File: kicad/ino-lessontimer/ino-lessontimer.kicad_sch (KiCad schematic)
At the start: 10 parts, among them SW1 BTNMinus, SW2 BTNPlus, SW3 BTNSet, SW4 BTNShow

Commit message: Updated schema to fixed TM1637
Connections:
- net +5V: now also U1.3 (VCC); no longer U1. (VCC)
- net GND: now also U1.4 (GND); no longer U1. (VCC)
- net at A1.5 (D2): now also U1.1 (CLK); no longer U1. (VCC)
- net at A1.6 (D3): now also U1.2 (DIO); no longer U1. (VCC)
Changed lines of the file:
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@@
     (stroke (width 0) (type default))
-  )
-  (symbol (lib_id "TM1637:TM1637") (at 107.95 73.66 0) (unit 1)
-    (in_bom yes) (on_board yes) (dnp no) (fields_autoplaced)
-    (property "Reference" "U1" (at 107.95 64.77 0)
-      (effects (font (size 1.27 1.27)))
-    )
-    (property "Value" "~" (at 107.95 73.66 0)
-      (effects (font (size 1.27 1.27)))
-    )
-    (property "Footprint" "" (at 107.95 73.66 0)
-      (effects (font (size 1.27 1.27)) hide)
-    )
-    (property "Datasheet" "" (at 107.95 73.66 0)
-      (effects (font (size 1.27 1.27)) hide)
-    )
-    (pin "")
-    (pin "")
-    (pin "")
-    (pin "")
-    (instances
-      (project "ino-lessontimer"
-        (path "/46ad6450-c889-484d-9737-a7f915eaad18"
-          (reference "U1") (unit 1)
-        )
-      )
-    )
   )
   (symbol (lib_id "Device:R") (at 107.95 101.6 90) (unit 1)
@@
         )
       )
+    )
+  )
+  (symbol (lib_id "TM1637:TM1637") (at 105.41 73.66 0) (unit 1)
+    (in_bom yes) (on_board yes) (dnp no) (fields_autoplaced)
+    (property "Reference" "U1" (at 105.41 64.77 0)
+      (effects (font (size 1.27 1.27)))
+    )
+    (property "Value" "~" (at 105.41 73.66 0)
+      (effects (font (size 1.27 1.27)))
+    )
+    (property "Footprint" "" (at 105.41 73.66 0)
+      (effects (font (size 1.27 1.27)) hide)
+    )
+    (property "Datasheet" "" (at 105.41 73.66 0)
+      (effects (font (size 1.27 1.27)) hide)
+    )
+    (pin "1")
+    (pin "2")
+    (pin "3")
+    (pin "4")
+    (instances
+      (project "ino-lessontimer"
+        (path "/46ad6450-c889-484d-9737-a7f915eaad18"
+          (reference "U1") (unit 1)
+        )
+      )

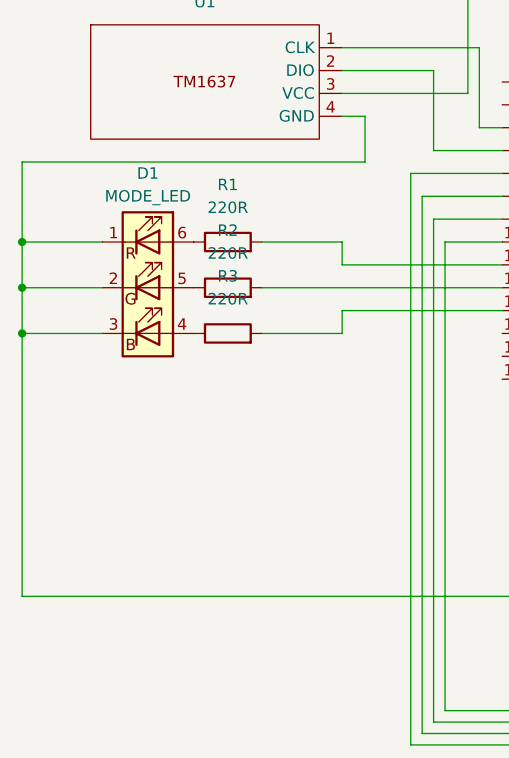
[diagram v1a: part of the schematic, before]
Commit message: Replaced MODE_LED symbol in the schema
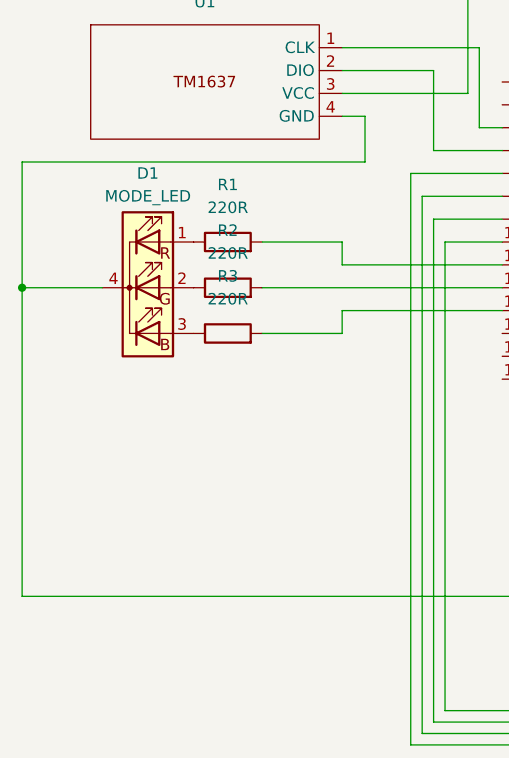
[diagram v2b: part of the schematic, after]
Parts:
- removed D1: MODE_LED, symbol Device:LED_RGB
- added D1: MODE_LED, symbol Device:LED_RGBK
- R1, R2, R3: footprint (none) -> Resistor_THT:R_Axial_DIN0207_L6.3mm_D2.5mm_P7.62mm_Horizontal
- SW1, SW2, SW3, SW4: footprint (none) -> Button_Switch_THT:Push_E-Switch_KS01Q01
- U1: footprint (none) -> TM1637:TM1637
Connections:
- net GND: now also D1.4 (K)
- net at R3.1: now also D1.3 (BA)
- net at R2.1: now also D1.2 (GA)
- net at R1.1: now also D1.1 (RA)
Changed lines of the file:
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@@
   (junction (at 199.39 104.14) (diameter 0) (color 0 0 0 0)
   )
-  (junction (at 85.09 91.44) (diameter 0) (color 0 0 0 0)
-  )
   (junction (at 199.39 115.57) (diameter 0) (color 0 0 0 0)
   )
-  (junction (at 85.09 101.6) (diameter 0) (color 0 0 0 0)
-  )
   (junction (at 199.39 125.73) (diameter 0) (color 0 0 0 0)
   )
@@
     (stroke (width 0) (type default))
   )
-  (wire (pts (xy 85.09 101.6) (xy 93.98 101.6))
-    (stroke (width 0) (type default))
-  )
   (wire (pts (xy 85.09 130.81) (xy 151.13 130.81))
     (stroke (width 0) (type default))
@@
     (stroke (width 0) (type default))
   )
-  (wire (pts (xy 85.09 82.55) (xy 85.09 91.44))
-    (stroke (width 0) (type default))
-  )
-  (wire (pts (xy 85.09 96.52) (xy 85.09 101.6))
-    (stroke (width 0) (type default))
-  )
   (wire (pts (xy 167.64 143.51) (xy 167.64 125.73))
     (stroke (width 0) (type default))
   )
-  (wire (pts (xy 85.09 91.44) (xy 85.09 96.52))
+  (wire (pts (xy 85.09 82.55) (xy 85.09 96.52))
     (stroke (width 0) (type default))
   )
@@
     (stroke (width 0) (type default))
   )
-  (wire (pts (xy 93.98 91.44) (xy 85.09 91.44))
-    (stroke (width 0) (type default))
-  )
   (wire (pts (xy 132.08 91.44) (xy 132.08 143.51))
     (stroke (width 0) (type default))
@@
     (stroke (width 0) (type default))
   )
-  (wire (pts (xy 85.09 101.6) (xy 85.09 130.81))
+  (wire (pts (xy 85.09 96.52) (xy 85.09 130.81))
     (stroke (width 0) (type default))
   )
@@
       (effects (font (size 1.27 1.27)))
     )
-    (property "Footprint" "" (at 107.95 103.378 90)
+    (property "Footprint" "Resistor_THT:R_Axial_DIN0207_L6.3mm_D2.5mm_P7.62mm_Horizontal" (at 107.95 103.378 90)
       (effects (font (size 1.27 1.27)) hide)
     )
@@
     )
   )
-  (symbol (lib_id "Device:LED_RGB") (at 99.06 96.52 0) (unit 1)
-    (in_bom yes) (on_board yes) (dnp no) (fields_autoplaced)
-    (property "Reference" "D1" (at 99.06 83.82 0)
-      (effects (font (size 1.27 1.27)))
-    )
-    (property "Value" "MODE_LED" (at 99.06 86.36 0)
-      (effects (font (size 1.27 1.27)))
-    )
-    (property "Footprint" "" (at 99.06 97.79 0)
-      (effects (font (size 1.27 1.27)) hide)
-    )
-    (property "Datasheet" "~" (at 99.06 97.79 0)
+  (symbol (lib_id "power:GND") (at 151.13 130.81 0) (unit 1)
+    (in_bom yes) (on_board yes) (dnp no) (fields_autoplaced)
+    (property "Reference" "#PWR02" (at 151.13 137.16 0)
+      (effects (font (size 1.27 1.27)) hide)
+    )
+    (property "Value" "GND" (at 151.13 135.89 0)
+      (effects (font (size 1.27 1.27)))
+    )
+    (property "Footprint" "" (at 151.13 130.81 0)
+      (effects (font (size 1.27 1.27)) hide)
+    )
+    (property "Datasheet" "" (at 151.13 130.81 0)
+      (effects (font (size 1.27 1.27)) hide)
+    )
+    (pin "1")
+    (instances
+      (project "ino-lessontimer"
+        (path "/46ad6450-c889-484d-9737-a7f915eaad18"
+          (reference "#PWR02") (unit 1)
+        )
+      )
+    )
+  )
+  (symbol (lib_id "Switch:SW_Push") (at 184.15 93.98 0) (unit 1)
+    (in_bom yes) (on_board yes) (dnp no) (fields_autoplaced)
+    (property "Reference" "SW1" (at 184.15 86.36 0)
+      (effects (font (size 1.27 1.27)))
+    )
+    (property "Value" "BTNMinus" (at 184.15 88.9 0)
+      (effects (font (size 1.27 1.27)))
+    )
+    (property "Footprint" "Button_Switch_THT:Push_E-Switch_KS01Q01" (at 184.15 88.9 0)
+      (effects (font (size 1.27 1.27)) hide)
+    )
+    (property "Datasheet" "~" (at 184.15 88.9 0)
+      (effects (font (size 1.27 1.27)) hide)
+    )
+    (pin "1")
+    (pin "2")
+    (instances
+      (project "ino-lessontimer"
+        (path "/46ad6450-c889-484d-9737-a7f915eaad18"
+          (reference "SW1") (unit 1)
+        )
+      )
+    )
+  )
+  (symbol (lib_id "TM1637:TM1637") (at 105.41 73.66 0) (unit 1)
+    (in_bom yes) (on_board yes) (dnp no) (fields_autoplaced)
+    (property "Reference" "U1" (at 105.41 64.77 0)
+      (effects (font (size 1.27 1.27)))
+    )
+    (property "Value" "~" (at 105.41 73.66 0)
+      (effects (font (size 1.27 1.27)))
+    )
+    (property "Footprint" "TM1637:TM1637" (at 105.41 73.66 0)
+      (effects (font (size 1.27 1.27)) hide)
+    )
+    (property "Datasheet" "" (at 105.41 73.66 0)
       (effects (font (size 1.27 1.27)) hide)
     )
@@
     (pin "3")
     (pin "4")
-    (pin "5")
-    (pin "6")
-    (instances
-      (project "ino-lessontimer"
-        (path "/46ad6450-c889-484d-9737-a7f915eaad18"
-          (reference "D1") (unit 1)
-        )
-      )
-    )
-  )
-  (symbol (lib_id "power:GND") (at 151.13 130.81 0) (unit 1)
-    (in_bom yes) (on_board yes) (dnp no) (fields_autoplaced)
-    (property "Reference" "#PWR02" (at 151.13 137.16 0)
-      (effects (font (size 1.27 1.27)) hide)
-    )
-    (property "Value" "GND" (at 151.13 135.89 0)
-      (effects (font (size 1.27 1.27)))
-    )
-    (property "Footprint" "" (at 151.13 130.81 0)
-      (effects (font (size 1.27 1.27)) hide)
-    )
-    (property "Datasheet" "" (at 151.13 130.81 0)
-      (effects (font (size 1.27 1.27)) hide)
-    )
-    (pin "1")
-    (instances
-      (project "ino-lessontimer"
-        (path "/46ad6450-c889-484d-9737-a7f915eaad18"
-          (reference "#PWR02") (unit 1)
-        )
-      )
-    )
-  )
-  (symbol (lib_id "Switch:SW_Push") (at 184.15 93.98 0) (unit 1)
-    (in_bom yes) (on_board yes) (dnp no) (fields_autoplaced)
-    (property "Reference" "SW1" (at 184.15 86.36 0)
-      (effects (font (size 1.27 1.27)))
-    )
-    (property "Value" "BTNMinus" (at 184.15 88.9 0)
-      (effects (font (size 1.27 1.27)))
-    )
-    (property "Footprint" "" (at 184.15 88.9 0)
-      (effects (font (size 1.27 1.27)) hide)
-    )
-    (property "Datasheet" "~" (at 184.15 88.9 0)
-      (effects (font (size 1.27 1.27)) hide)
-    )
-    (pin "1")
-    (pin "2")
-    (instances
-      (project "ino-lessontimer"
-        (path "/46ad6450-c889-484d-9737-a7f915eaad18"
-          (reference "SW1") (unit 1)
-        )
-      )
-    )
-  )
-  (symbol (lib_id "TM1637:TM1637") (at 105.41 73.66 0) (unit 1)
-    (in_bom yes) (on_board yes) (dnp no) (fields_autoplaced)
-    (property "Reference" "U1" (at 105.41 64.77 0)
-      (effects (font (size 1.27 1.27)))
-    )
-    (property "Value" "~" (at 105.41 73.66 0)
-      (effects (font (size 1.27 1.27)))
-    )
-    (property "Footprint" "" (at 105.41 73.66 0)
-      (effects (font (size 1.27 1.27)) hide)
-    )
-    (property "Datasheet" "" (at 105.41 73.66 0)
-      (effects (font (size 1.27 1.27)) hide)
-    )
-    (pin "1")
-    (pin "2")
-    (pin "3")
-    (pin "4")
     (instances
       (project "ino-lessontimer"
@@
       (effects (font (size 1.27 1.27)))
     )
-    (property "Footprint" "" (at 107.95 98.298 90)
+    (property "Footprint" "Resistor_THT:R_Axial_DIN0207_L6.3mm_D2.5mm_P7.62mm_Horizontal" (at 107.95 98.298 90)
       (effects (font (size 1.27 1.27)) hide)
     )
@@
       (effects (font (size 1.27 1.27)))
     )
-    (property "Footprint" "" (at 107.95 93.218 90)
+    (property "Footprint" "Resistor_THT:R_Axial_DIN0207_L6.3mm_D2.5mm_P7.62mm_Horizontal" (at 107.95 93.218 90)
       (effects (font (size 1.27 1.27)) hide)
     )
@@
     )
   )
+  (symbol (lib_id "Device:LED_RGBK") (at 99.06 96.52 0) (unit 1)
+    (in_bom yes) (on_board yes) (dnp no) (fields_autoplaced)
+    (property "Reference" "D1" (at 99.06 83.82 0)
+      (effects (font (size 1.27 1.27)))
+    )
+    (property "Value" "MODE_LED" (at 99.06 86.36 0)
+      (effects (font (size 1.27 1.27)))
+    )
+    (property "Footprint" "" (at 99.06 97.79 0)
+      (effects (font (size 1.27 1.27)) hide)
+    )
+    (property "Datasheet" "~" (at 99.06 97.79 0)
+      (effects (font (size 1.27 1.27)) hide)
+    )
+    (pin "1")
+    (pin "2")
+    (pin "3")
+    (pin "4")
+    (instances
+      (project "ino-lessontimer"
+        (path "/46ad6450-c889-484d-9737-a7f915eaad18"
+          (reference "D1") (unit 1)
+        )
+      )
+    )
+  )
   (symbol (lib_id "Switch:SW_Push") (at 184.15 115.57 0) (unit 1)
     (in_bom yes) (on_board yes) (dnp no) (fields_autoplaced)
@@
       (effects (font (size 1.27 1.27)))
     )
-    (property "Footprint" "" (at 184.15 110.49 0)
+    (property "Footprint" "Button_Switch_THT:Push_E-Switch_KS01Q01" (at 184.15 110.49 0)
       (effects (font (size 1.27 1.27)) hide)
     )
@@
       (effects (font (size 1.27 1.27)))
     )
-    (property "Footprint" "" (at 184.15 120.65 0)
+    (property "Footprint" "Button_Switch_THT:Push_E-Switch_KS01Q01" (at 184.15 120.65 0)
       (effects (font (size 1.27 1.27)) hide)
     )
@@
       (effects (font (size 1.27 1.27)))
     )
-    (property "Footprint" "" (at 184.15 99.06 0)
-      (effects (font (size 1.27 1.27)) hide)
-    )
+    (property "Footprint" "Button_Switch_THT:Push_E-Switch_KS01Q01" (at 184.15 99.06 0)
+      (effects (font (size 1.27 1.27)) hide)
+    )

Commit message: Added PCB
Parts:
- removed D1: MODE_LED, symbol Device:LED_RGBK
- added D1: LED_RKGB, LED_THT:LED_D5.0mm-4_RGB, symbol Device:LED_RKGB
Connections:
- net GND: now also A1.29 (GND), D1.2 (K)
- net at R3.1: now also D1.4 (BA)
- net at R2.1: now also D1.3 (GA)
- net at R1.1: now also D1.1 (RA)
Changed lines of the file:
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@@
   (junction (at 199.39 104.14) (diameter 0) (color 0 0 0 0)
   )
+  (junction (at 151.13 114.3) (diameter 0) (color 0 0 0 0)
+  )
   (junction (at 199.39 115.57) (diameter 0) (color 0 0 0 0)
   )
@@
   )
   (wire (pts (xy 85.09 96.52) (xy 85.09 130.81))
+    (stroke (width 0) (type default))
+  )
+  (wire (pts (xy 151.13 114.3) (xy 153.67 114.3))
     (stroke (width 0) (type default))
   )
@@
     )
   )
-  (symbol (lib_id "Device:LED_RGBK") (at 99.06 96.52 0) (unit 1)
+  (symbol (lib_id "Switch:SW_Push") (at 184.15 115.57 0) (unit 1)
+    (in_bom yes) (on_board yes) (dnp no) (fields_autoplaced)
+    (property "Reference" "SW3" (at 184.15 107.95 0)
+      (effects (font (size 1.27 1.27)))
+    )
+    (property "Value" "BTNSet" (at 184.15 110.49 0)
+      (effects (font (size 1.27 1.27)))
+    )
+    (property "Footprint" "Button_Switch_THT:Push_E-Switch_KS01Q01" (at 184.15 110.49 0)
+      (effects (font (size 1.27 1.27)) hide)
+    )
+    (property "Datasheet" "~" (at 184.15 110.49 0)
+      (effects (font (size 1.27 1.27)) hide)
+    )
+    (pin "1")
+    (pin "2")
+    (instances
+      (project "ino-lessontimer"
+        (path "/46ad6450-c889-484d-9737-a7f915eaad18"
+          (reference "SW3") (unit 1)
+        )
+      )
+    )
+  )
+  (symbol (lib_id "Switch:SW_Push") (at 184.15 125.73 0) (unit 1)
+    (in_bom yes) (on_board yes) (dnp no) (fields_autoplaced)
+    (property "Reference" "SW4" (at 184.15 118.11 0)
+      (effects (font (size 1.27 1.27)))
+    )
+    (property "Value" "BTNShow" (at 184.15 120.65 0)
+      (effects (font (size 1.27 1.27)))
+    )
+    (property "Footprint" "Button_Switch_THT:Push_E-Switch_KS01Q01" (at 184.15 120.65 0)
+      (effects (font (size 1.27 1.27)) hide)
+    )
+    (property "Datasheet" "~" (at 184.15 120.65 0)
+      (effects (font (size 1.27 1.27)) hide)
+    )
+    (pin "1")
+    (pin "2")
+    (instances
+      (project "ino-lessontimer"
+        (path "/46ad6450-c889-484d-9737-a7f915eaad18"
+          (reference "SW4") (unit 1)
+        )
+      )
+    )
+  )
+  (symbol (lib_id "Switch:SW_Push") (at 184.15 104.14 0) (unit 1)
+    (in_bom yes) (on_board yes) (dnp no) (fields_autoplaced)
+    (property "Reference" "SW2" (at 184.15 96.52 0)
+      (effects (font (size 1.27 1.27)))
+    )
+    (property "Value" "BTNPlus" (at 184.15 99.06 0)
+      (effects (font (size 1.27 1.27)))
+    )
+    (property "Footprint" "Button_Switch_THT:Push_E-Switch_KS01Q01" (at 184.15 99.06 0)
+      (effects (font (size 1.27 1.27)) hide)
+    )
+    (property "Datasheet" "~" (at 184.15 99.06 0)
+      (effects (font (size 1.27 1.27)) hide)
+    )
+    (pin "1")
+    (pin "2")
+    (instances
+      (project "ino-lessontimer"
+        (path "/46ad6450-c889-484d-9737-a7f915eaad18"
+          (reference "SW2") (unit 1)
+        )
+      )
+    )
+  )
+  (symbol (lib_id "power:+5V") (at 156.21 57.15 0) (unit 1)
+    (in_bom yes) (on_board yes) (dnp no) (fields_autoplaced)
+    (property "Reference" "#PWR01" (at 156.21 60.96 0)
+      (effects (font (size 1.27 1.27)) hide)
+    )
+    (property "Value" "+5V" (at 156.21 52.07 0)
+      (effects (font (size 1.27 1.27)))
+    )
+    (property "Footprint" "" (at 156.21 57.15 0)
+      (effects (font (size 1.27 1.27)) hide)
+    )
+    (property "Datasheet" "" (at 156.21 57.15 0)
+      (effects (font (size 1.27 1.27)) hide)
+    )
+    (pin "1")
+    (instances
+      (project "ino-lessontimer"
+        (path "/46ad6450-c889-484d-9737-a7f915eaad18"
+          (reference "#PWR01") (unit 1)
+        )
+      )
+    )
+  )
+  (symbol (lib_id "Device:LED_RKGB") (at 99.06 96.52 0) (unit 1)
     (in_bom yes) (on_board yes) (dnp no) (fields_autoplaced)
     (property "Reference" "D1" (at 99.06 83.82 0)
       (effects (font (size 1.27 1.27)))
     )
-    (property "Value" "MODE_LED" (at 99.06 86.36 0)
-      (effects (font (size 1.27 1.27)))
-    )
-    (property "Footprint" "" (at 99.06 97.79 0)
+    (property "Value" "LED_RKGB" (at 99.06 86.36 0)
+      (effects (font (size 1.27 1.27)))
+    )
+    (property "Footprint" "LED_THT:LED_D5.0mm-4_RGB" (at 99.06 97.79 0)
       (effects (font (size 1.27 1.27)) hide)
     )
@@
         )
       )
-    )
-  )
-  (symbol (lib_id "Switch:SW_Push") (at 184.15 115.57 0) (unit 1)
-    (in_bom yes) (on_board yes) (dnp no) (fields_autoplaced)
-    (property "Reference" "SW3" (at 184.15 107.95 0)
-      (effects (font (size 1.27 1.27)))
-    )
-    (property "Value" "BTNSet" (at 184.15 110.49 0)
-      (effects (font (size 1.27 1.27)))
-    )
-    (property "Footprint" "Button_Switch_THT:Push_E-Switch_KS01Q01" (at 184.15 110.49 0)
-      (effects (font (size 1.27 1.27)) hide)
-    )
-    (property "Datasheet" "~" (at 184.15 110.49 0)
-      (effects (font (size 1.27 1.27)) hide)
-    )
-    (pin "1")
-    (pin "2")
-    (instances
-      (project "ino-lessontimer"
-        (path "/46ad6450-c889-484d-9737-a7f915eaad18"
-          (reference "SW3") (unit 1)
-        )
-      )
-    )
-  )
-  (symbol (lib_id "Switch:SW_Push") (at 184.15 125.73 0) (unit 1)
-    (in_bom yes) (on_board yes) (dnp no) (fields_autoplaced)
-    (property "Reference" "SW4" (at 184.15 118.11 0)
-      (effects (font (size 1.27 1.27)))
-    )
-    (property "Value" "BTNShow" (at 184.15 120.65 0)
-      (effects (font (size 1.27 1.27)))
-    )
-    (property "Footprint" "Button_Switch_THT:Push_E-Switch_KS01Q01" (at 184.15 120.65 0)
-      (effects (font (size 1.27 1.27)) hide)
-    )
-    (property "Datasheet" "~" (at 184.15 120.65 0)
-      (effects (font (size 1.27 1.27)) hide)
-    )
-    (pin "1")
-    (pin "2")
-    (instances
-      (project "ino-lessontimer"
-        (path "/46ad6450-c889-484d-9737-a7f915eaad18"
-          (reference "SW4") (unit 1)
-        )
-      )
-    )
-  )
-  (symbol (lib_id "Switch:SW_Push") (at 184.15 104.14 0) (unit 1)
-    (in_bom yes) (on_board yes) (dnp no) (fields_autoplaced)
-    (property "Reference" "SW2" (at 184.15 96.52 0)
-      (effects (font (size 1.27 1.27)))
-    )
-    (property "Value" "BTNPlus" (at 184.15 99.06 0)
-      (effects (font (size 1.27 1.27)))
-    )
-    (property "Footprint" "Button_Switch_THT:Push_E-Switch_KS01Q01" (at 184.15 99.06 0)
-      (effects (font (size 1.27 1.27)) hide)
-    )
-    (property "Datasheet" "~" (at 184.15 99.06 0)
-      (effects (font (size 1.27 1.27)) hide)
-    )
-    (pin "1")
-    (pin "2")
-    (instances
-      (project "ino-lessontimer"
-        (path "/46ad6450-c889-484d-9737-a7f915eaad18"
-          (reference "SW2") (unit 1)
-        )
-      )
-    )
-  )
-  (symbol (lib_id "power:+5V") (at 156.21 57.15 0) (unit 1)
-    (in_bom yes) (on_board yes) (dnp no) (fields_autoplaced)
-    (property "Reference" "#PWR01" (at 156.21 60.96 0)
-      (effects (font (size 1.27 1.27)) hide)
-    )
-    (property "Value" "+5V" (at 156.21 52.07 0)
-      (effects (font (size 1.27 1.27)))
-    )
-    (property "Footprint" "" (at 156.21 57.15 0)
-      (effects (font (size 1.27 1.27)) hide)
-    )
-    (property "Datasheet" "" (at 156.21 57.15 0)
-      (effects (font (size 1.27 1.27)) hide)
-    )
-    (pin "1")
-    (instances
-      (project "ino-lessontimer"
-        (path "/46ad6450-c889-484d-9737-a7f915eaad18"
-          (reference "#PWR01") (unit 1)
-        )
-      )
